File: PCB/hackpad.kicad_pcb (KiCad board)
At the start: 2 copper layers, 79 x 99 mm, 53 parts, among them J1 Conn_01x04, SW1 SW_Push, SW10 SW_Push, SW11 SW_Push, SW12 SW_Push, SW13 SW_Push, SW14 SW_Push, SW15 SW_Push, SW16 SW_Push, SW2 SW_Push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

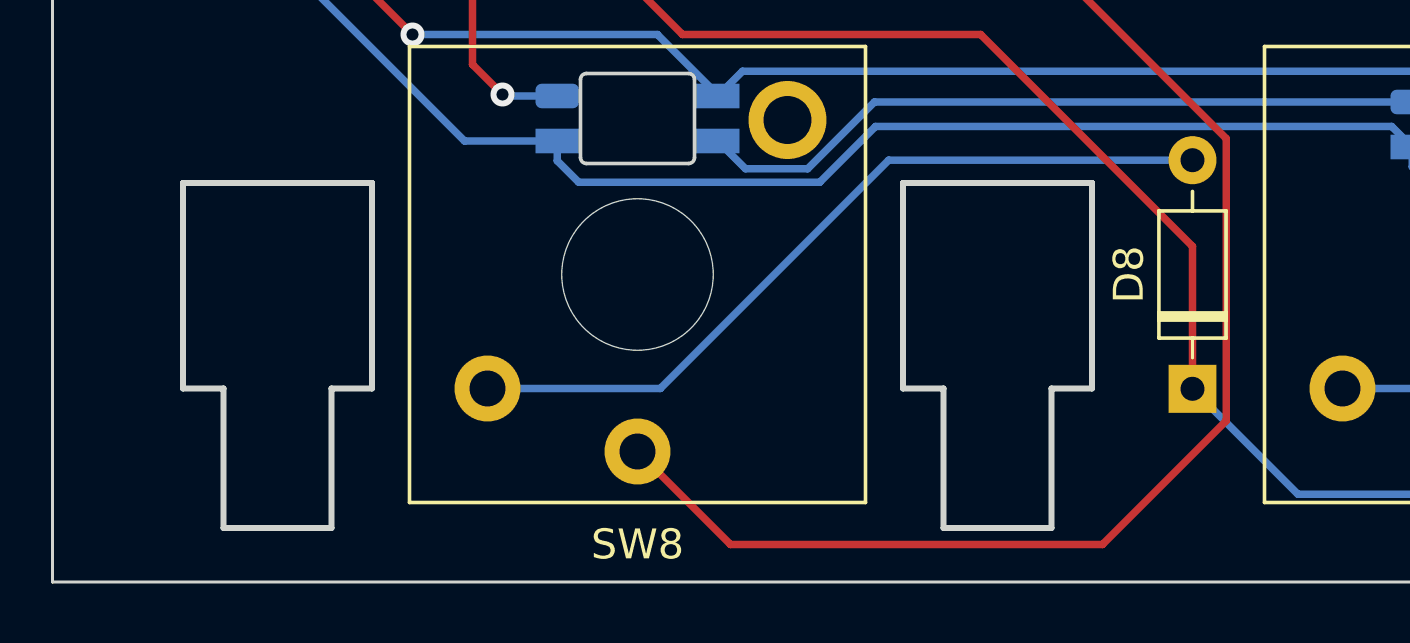
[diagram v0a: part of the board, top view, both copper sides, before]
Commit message: update pcb with new footprint for stabilizer
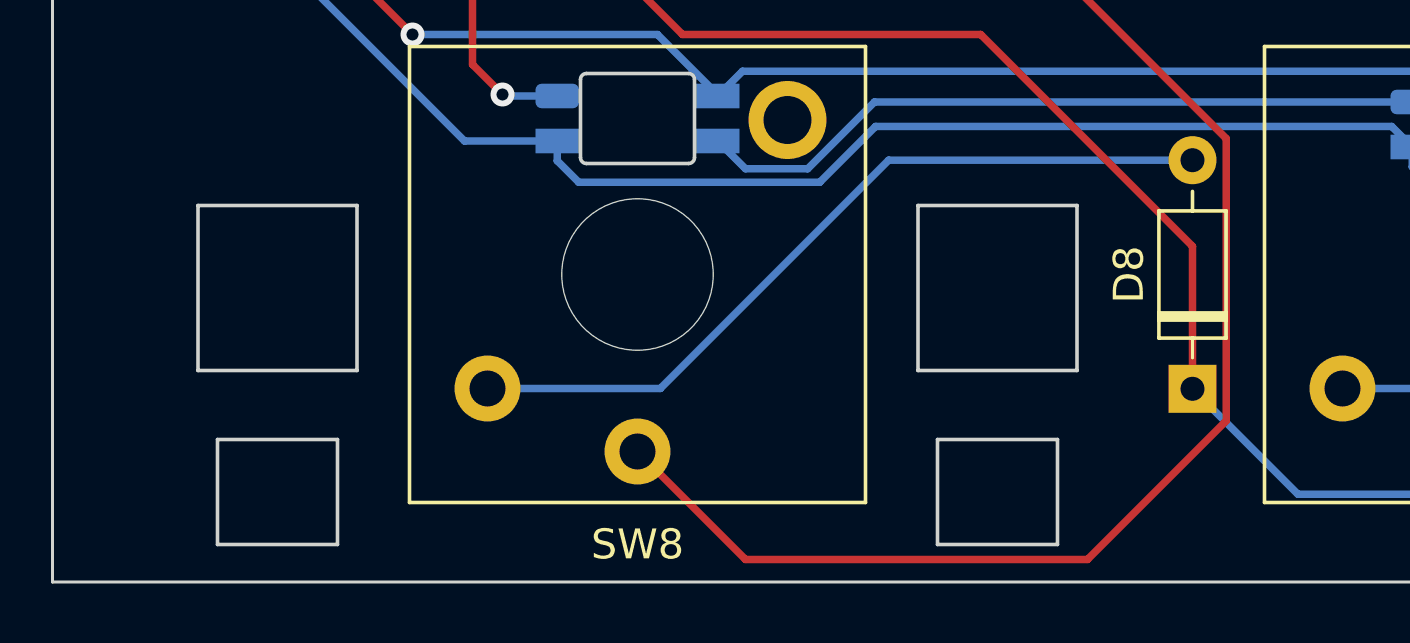
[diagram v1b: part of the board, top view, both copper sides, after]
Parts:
- removed Kailh PG1350: Choc, Keebio-Parts:Kailh-PG1350-Stab-Cutout
- added 2u: , mbk-footprints:Choc-2u-solder, F.Cu at (92.5, 130.0)
